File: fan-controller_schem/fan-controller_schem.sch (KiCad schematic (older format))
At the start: 0 parts

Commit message: Communication system
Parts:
- added J101: Transformer, symbol Screw_Terminal_1x03
- added J102: Mains, symbol Screw_Terminal_1x03
- added J103: MAINS_SW, symbol Screw_Terminal_1x03
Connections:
- new net PSU/18VAC_IN_A: J101.1
- new net PSU/18VAC_IN_B: J101.3
- new net PSU/18VAC_IN_MID: J101.2
- new net PSU/L_IN: J102.1
- new net PSU/L_OUT: J103.1
- new net PSU/N_IN: J102.2
- new net PSU/N_OUT: J103.2
- new net PSU/PE_IN: J102.3
- new net PSU/PE_OUT: J103.3
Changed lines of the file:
@@
 EESchema Schematic File Version 2
-LIBS:power
+LIBS:fan-controller_parts
 LIBS:device
-LIBS:transistors
-LIBS:conn
-LIBS:linear
-LIBS:regul
+LIBS:74xgxx
 LIBS:74xx
-LIBS:cmos4000
-LIBS:adc-dac
-LIBS:memory
-LIBS:xilinx
-LIBS:microcontrollers
-LIBS:dsp
-LIBS:microchip
-LIBS:analog_switches
-LIBS:motorola
-LIBS:texas
-LIBS:intel
-LIBS:audio
-LIBS:interface
-LIBS:digital-audio
-LIBS:philips
-LIBS:display
-LIBS:cypress
-LIBS:siliconi
-LIBS:opto
-LIBS:atmel
-LIBS:contrib
-LIBS:valves
-LIBS:74xgxx
 LIBS:ac-dc
 LIBS:actel
+LIBS:adc-dac
 LIBS:allegro
 LIBS:Altera
 LIBS:analog_devices
+LIBS:analog_switches
+LIBS:atmel
+LIBS:audio
 LIBS:battery_management
 LIBS:bbd
 LIBS:bosch
 LIBS:brooktre
+LIBS:cmos4000
 LIBS:cmos_ieee
+LIBS:conn
+LIBS:contrib
+LIBS:cypress
 LIBS:dc-dc
+LIBS:digital-audio
 LIBS:diode
+LIBS:display
+LIBS:dsp
 LIBS:elec-unifil
 LIBS:ESD_Protection
@@
 LIBS:graphic
 LIBS:hc11
+LIBS:infineon
+LIBS:intel
+LIBS:interface
+LIBS:intersil
 LIBS:ir
 LIBS:Lattice
 LIBS:leds
+LIBS:LEM
+LIBS:linear
 LIBS:logo
 LIBS:maxim
 LIBS:mechanical
+LIBS:memory
+LIBS:microchip
 LIBS:microchip_dspic33dsc
 LIBS:microchip_pic10mcu
@@
 LIBS:microchip_pic24mcu
 LIBS:microchip_pic32mcu
+LIBS:microcontrollers
 LIBS:modules
 LIBS:motor_drivers
+LIBS:motorola
 LIBS:motors
 LIBS:msp430
@@
 LIBS:nxp_armmcu
 LIBS:onsemi
+LIBS:opto
 LIBS:Oscillators
+LIBS:philips
+LIBS:power
 LIBS:powerint
 LIBS:Power_Management
 LIBS:pspice
 LIBS:references
+LIBS:regul
 LIBS:relays
 LIBS:rfcom
+LIBS:RFSolutions
 LIBS:sensors
 LIBS:silabs
+LIBS:siliconi
 LIBS:stm8
 LIBS:stm32
 LIBS:supertex
 LIBS:switches
+LIBS:texas
 LIBS:transf
+LIBS:transistors
 LIBS:triac_thyristor
 LIBS:ttl_ieee
+LIBS:valves
 LIBS:video
 LIBS:wiznet
 LIBS:Worldsemi
 LIBS:Xicor
+LIBS:xilinx
 LIBS:zetex
 LIBS:Zilog
@@
 EELAYER 25 0
 EELAYER END
-$Descr A4 11693 8268
+$Descr A3 16535 11693
 encoding utf-8
-Sheet 1 6
+Sheet 1 10
 Title "Main_Board"
 Date "2017-04-15"
@@
 $EndDescr
 $Sheet
-S 1950 950  1000 1350
-U 58F1C440
-F0 "psu" 60
-F1 "psu.sch" 60
-F2 "V_Relay" O R 2950 1750 60
-F3 "V_Contr" O R 2950 1900 60
-F4 "GND" U R 2950 2150 60
-F5 "L" I L 1950 1100 60
-F6 "N" I L 1950 1250 60
-F7 "L_Fan_Out" O R 2950 1100 60
-F8 "N_Fan_Out" O R 2950 1250 60
-F9 "E_Fan" U R 2950 1400 60
-F10 "E" U L 1950 1400 60
+S 1950 1300 1650 1350
+U 592E7843
+F0 "PSU" 60
+F1 "subcircuits/psu.sch" 60
+F2 "18VAC_IN_A" U L 1950 1450 60
+F3 "18VAC_IN_MID" U L 1950 1550 60
+F4 "18VAC_IN_B" U L 1950 1650 60
+F5 "V_15V_CC_OUT" U R 3600 1450 60
+F6 "V_15V_EE_OUT" U R 3600 1550 60
+F7 "GND" U R 3600 1800 60
+F8 "PE_OUT" U R 3600 2500 60
+F9 "L_OUT" U R 3600 2300 60
+F10 "FAN_ON" I R 3600 1950 60
+F11 "L_IN" U L 1950 2300 60
+F12 "N_IN" U L 1950 2400 60
+F13 "PE_IN" U L 1950 2500 60
+F14 "N_OUT" U R 3600 2400 60
+F15 "V_5V_OUT" U R 3600 1650 60
 $EndSheet
+$Comp
+L Screw_Terminal_1x03 J101
+U 1 1 59325FBC
+P 1400 1550
+F 0 "J101" H 1400 1900 50  0000 C TNN
+F 1 "Transformer" V 1250 1550 50  0000 C TNN
+F 2 "" H 1400 1225 50  0001 C CNN
+F 3 "" H 1375 1650 50  0001 C CNN
+	1    1400 1550
+	1    0    0    -1
+$EndComp
+Wire Wire Line
+	1600 1550 1950 1550
+Wire Wire Line
+	1950 1450 1850 1450
+Wire Wire Line
+	1850 1450 1850 1350
+Wire Wire Line
+	1850 1350 1600 1350
+Wire Wire Line
+	1950 1650 1850 1650
+Wire Wire Line
+	1850 1650 1850 1750
+Wire Wire Line
+	1850 1750 1600 1750
+$Comp
+L Screw_Terminal_1x03 J102
+U 1 1 593262DA
+P 1400 2400
+F 0 "J102" H 1400 2750 50  0000 C TNN
+F 1 "Mains" V 1250 2400 50  0000 C TNN
+F 2 "" H 1400 2075 50  0001 C CNN
+F 3 "" H 1375 2500 50  0001 C CNN
+	1    1400 2400
+	1    0    0    -1
+$EndComp
+Wire Wire Line
+	1600 2200 1850 2200
+Wire Wire Line
+	1850 2200 1850 2300
+Wire Wire Line
+	1850 2300 1950 2300
+Wire Wire Line
+	1600 2600 1850 2600
+Wire Wire Line
+	1850 2600 1850 2500
+Wire Wire Line
+	1850 2500 1950 2500
+Wire Wire Line
+	1600 2400 1950 2400
+$Comp
+L Screw_Terminal_1x03 J103
+U 1 1 59326420
+P 4200 2400
+F 0 "J103" H 4200 2750 50  0000 C TNN
+F 1 "MAINS_SW" V 4050 2400 50  0000 C TNN
+F 2 "" H 4200 2075 50  0001 C CNN
+F 3 "" H 4175 2500 50  0001 C CNN
+	1    4200 2400
+	-1   0    0    -1
+$EndComp
+Wire Wire Line
+	3600 2400 4000 2400
+Wire Wire Line
+	3600 2300 3700 2300
+Wire Wire Line
+	3700 2300 3700 2200
+Wire Wire Line
+	3700 2200 4000 2200
+Wire Wire Line
+	3600 2500 3700 2500
+Wire Wire Line
+	3700 2500 3700 2600
+Wire Wire Line
+	3700 2600 4000 2600
 $Sheet
-S 7350 950  1350 1350
-U 58F2AC58
-F0 "fan_driver" 60
-F1 "fan_driver.sch" 60
-F2 "L_Fan_in" I L 7350 1100 60
-F3 "N_Fan_In" I L 7350 1250 60
-F4 "L_Fan_Out" O R 8700 1100 60
-F5 "N_Fan_Out" O R 8700 1250 60
-F6 "V_Relay" I L 7350 1750 60
-F7 "GND" U L 7350 2150 60
-F8 "In" I L 7350 1900 60
-F9 "E_Fan" U L 7350 1400 60
-F10 "E_Fan" U R 8700 1400 60
+S 12200 1300 1850 1350
+U 593761B7
+F0 "power-amp" 60
+F1 "subcircuits/power-amp.sch" 60
+F2 "SIG_IN" I L 12200 2000 60
+F3 "VCC" U L 12200 1450 60
+F4 "VEE" U L 12200 1550 60
+F5 "GND" U L 12200 1650 60
+F6 "SIG_OUT" O R 14050 2000 60
 $EndSheet
+Wire Wire Line
+	3600 1450 12200 1450
+Wire Wire Line
+	3600 1550 12200 1550
+Wire Wire Line
+	3600 1800 12000 1800
+Wire Wire Line
+	12000 1800 12000 1650
+Wire Wire Line
+	12000 1650 12200 1650
 $Sheet
-S 6100 3550 2600 1150
-U 58F2B243
-F0 "ui_driver" 60
-F1 "ui_driver.sch" 60
+S 7600 2300 2350 1700
+U 5934A3ED
+F0 "comms" 60
+F1 "subcircuits/comms.sch" 60
+F2 "VCC" U L 7600 2450 60
+F3 "VEE" U L 7600 2600 60
+F4 "GND" U L 7600 2750 60
 $EndSheet
-$Sheet
-S 4000 3550 1700 1250
-U 58F2B324
-F0 "controller" 60
-F1 "controller.sch" 60
-$EndSheet
-Wire Wire Line
-	2950 1100 7350 1100
-Wire Wire Line
-	2950 1250 7350 1250
-Wire Wire Line
-	2950 1400 7350 1400
-Wire Wire Line
-	2950 1750 7350 1750
-Wire Wire Line
-	2950 2150 7350 2150
-$Sheet
-S 1950 3550 1450 800
-U 58F345A2
-F0 "sensor_interface" 60
-F1 "sensor_interface.sch" 60
-F2 "SDA_In" B L 1950 3850 60
-F3 "SCL_In" B L 1950 4050 60
-F4 "GND_In" U L 1950 4250 60
-F5 "V_Contr_In" I L 1950 3650 60
-F6 "VCC_Sens_Out" O R 3400 3650 60
-F7 "GND_Out" U R 3400 4250 60
-F8 "SCL_out" B R 3400 4050 60
-F9 "SDA_out" B R 3400 3850 60
-$EndSheet
+Wire Wire Line
+	7600 2450 7300 2450
+Wire Wire Line
+	7300 2450 7300 1450
+Connection ~ 7300 1450
+Wire Wire Line
+	7600 2600 7200 2600
+Wire Wire Line
+	7200 2600 7200 1550
+Connection ~ 7200 1550
+Wire Wire Line
+	7600 2750 7100 2750
+Wire Wire Line
+	7100 2750 7100 1800
+Connection ~ 7100 1800
 $EndSCHEMATC

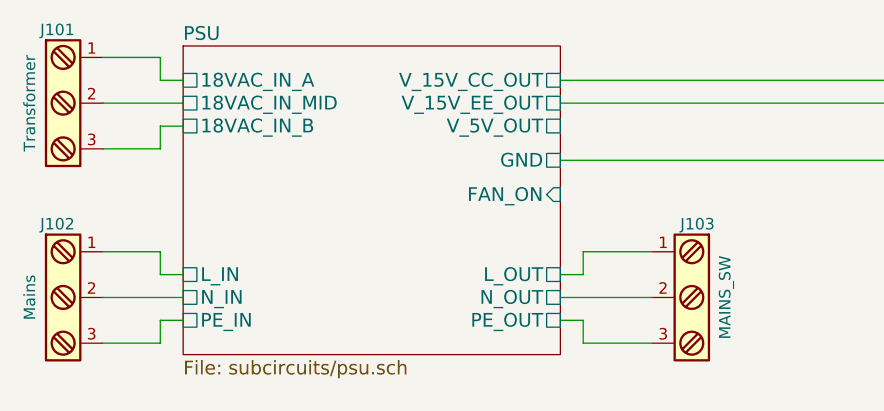
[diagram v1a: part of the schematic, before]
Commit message: Reorganized drawings. Writing documentation.
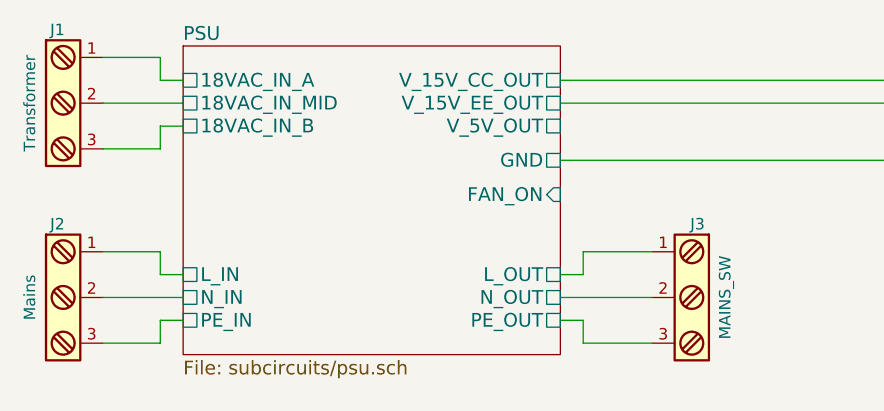
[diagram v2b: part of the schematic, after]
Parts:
- renumbered J101 to J1, J102 to J2, J103 to J3
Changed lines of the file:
@@
 LIBS:graphic
 LIBS:hc11
-LIBS:infineon
 LIBS:intel
 LIBS:interface
-LIBS:intersil
 LIBS:ir
 LIBS:Lattice
 LIBS:leds
-LIBS:LEM
 LIBS:linear
 LIBS:logo
@@
 LIBS:relays
 LIBS:rfcom
-LIBS:RFSolutions
 LIBS:sensors
 LIBS:silabs
@@
 $EndSheet
 $Comp
-L Screw_Terminal_1x03 J101
+L Screw_Terminal_1x03 J1
 U 1 1 59325FBC
 P 1400 1550
-F 0 "J101" H 1400 1900 50  0000 C TNN
+F 0 "J1" H 1400 1900 50  0000 C TNN
 F 1 "Transformer" V 1250 1550 50  0000 C TNN
 F 2 "" H 1400 1225 50  0001 C CNN
@@
 	1850 1750 1600 1750
 $Comp
-L Screw_Terminal_1x03 J102
+L Screw_Terminal_1x03 J2
 U 1 1 593262DA
 P 1400 2400
-F 0 "J102" H 1400 2750 50  0000 C TNN
+F 0 "J2" H 1400 2750 50  0000 C TNN
 F 1 "Mains" V 1250 2400 50  0000 C TNN
 F 2 "" H 1400 2075 50  0001 C CNN
@@
 	1600 2400 1950 2400
 $Comp
-L Screw_Terminal_1x03 J103
+L Screw_Terminal_1x03 J3
 U 1 1 59326420
 P 4200 2400
-F 0 "J103" H 4200 2750 50  0000 C TNN
+F 0 "J3" H 4200 2750 50  0000 C TNN
 F 1 "MAINS_SW" V 4050 2400 50  0000 C TNN
 F 2 "" H 4200 2075 50  0001 C CNN
